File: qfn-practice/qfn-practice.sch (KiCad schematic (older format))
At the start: 5 parts, among them IC1 CY8C4245LQI-483, J1 Conn_01x10, J2 Conn_01x10, U1 ATtiny85-20MU, U2 STM32F031G4Ux

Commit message: map attiny pins to stm32 footprint
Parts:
- removed IC1: CY8C4245LQI-483, SamacSys_Parts:QFN50P600X600X60-41N-D, symbol SamacSys_Parts:CY8C4245LQI-483
- removed U1: ATtiny85-20MU, Package_DFN_QFN:QFN-20-1EP_4x4mm_P0.5mm_EP2.6x2.6mm, symbol MCU_Microchip_ATtiny:ATtiny85-20MU
- removed U2: STM32F031G4Ux, Package_DFN_QFN:QFN-28_4x4mm_P0.5mm, symbol MCU_ST_STM32F0:STM32F031G4Ux
- added U2: STM32F031G4Ux-thermal-pad, SamacSys_Parts:QFN28-4x4mm-0_5mmP-thermalpad, symbol SamacSys_Parts:STM32F031G4Ux-thermal-pad
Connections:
- net labels added: AT_GND_ST_PA5, AT_PB0_ST_GND, AT_PB1_ST_VDD, AT_PB2_ST_PA9, AT_PB3_ST_PF1, AT_PB4_ST_PA0, AT_PB5_ST_PF0, AT_VCC_ST_PA10
- wire segments 24 -> 33
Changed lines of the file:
@@
 $EndDescr
-$Comp
-L MCU_Microchip_ATtiny:ATtiny85-20MU U1
-U 1 1 60477C1D
-P 3050 1950
-F 0 "U1" H 2507 1996 50  0000 R CNN
-F 1 "ATtiny85-20MU" H 2507 1905 50  0000 R CNN
-F 2 "Package_DFN_QFN:QFN-20-1EP_4x4mm_P0.5mm_EP2.6x2.6mm" H 3050 1950 50  0001 C CIN
-F 3 "http://ww1.microchip.com/downloads/en/DeviceDoc/atmel-2586-avr-8-bit-microcontroller-attiny25-attiny45-attiny85_datasheet.pdf" H 3050 1950 50  0001 C CNN
-	1    3050 1950
-	1    0    0    -1
-$EndComp
-$Comp
-L MCU_ST_STM32F0:STM32F031G4Ux U2
-U 1 1 60479D04
-P 7150 3050
-F 0 "U2" H 7350 2100 50  0000 C CNN
-F 1 "STM32F031G4Ux" H 7600 2000 50  0000 C CNN
-F 2 "Package_DFN_QFN:QFN-28_4x4mm_P0.5mm" H 6750 2250 50  0001 R CNN
-F 3 "http://www.st.com/st-web-ui/static/active/en/resource/technical/document/datasheet/DM00104043.pdf" H 7150 3050 50  0001 C CNN
-	1    7150 3050
-	1    0    0    -1
-$EndComp
-$Comp
-L SamacSys_Parts:CY8C4245LQI-483 IC1
-U 1 1 6047907D
-P 2750 4900
-F 0 "IC1" H 4794 4496 50  0000 L CNN
-F 1 "CY8C4245LQI-483" H 4794 4405 50  0000 L CNN
-F 2 "SamacSys_Parts:QFN50P600X600X60-41N-D" H 4600 5700 50  0001 L CNN
-F 3 "http://www.cypress.com/file/138656/download.pdf" H 4600 5600 50  0001 L CNN
-F 4 "ARM Microcontrollers - MCU 32KB Flash 4KB SRAM PSoC 4" H 4600 5500 50  0001 L CNN "Description"
-F 5 "0.6" H 4600 5400 50  0001 L CNN "Height"
-F 6 "727-CY8C4245LQI-483" H 4600 5300 50  0001 L CNN "Mouser Part Number"
-F 7 "https://www.mouser.co.uk/ProductDetail/Cypress-Semiconductor/CY8C4245LQI-483?qs=LqwxS8kK3AsOWZFbGGtkOg%3D%3D" H 4600 5200 50  0001 L CNN "Mouser Price/Stock"
-F 8 "Cypress Semiconductor" H 4600 5100 50  0001 L CNN "Manufacturer_Name"
-F 9 "CY8C4245LQI-483" H 4600 5000 50  0001 L CNN "Manufacturer_Part_Number"
-	1    2750 4900
-	1    0    0    -1
-$EndComp
-$Comp
-L power:+3.3V #PWR0101
-U 1 1 6047A94E
-P 3050 1350
-F 0 "#PWR0101" H 3050 1200 50  0001 C CNN
-F 1 "+3.3V" H 3065 1523 50  0000 C CNN
-F 2 "" H 3050 1350 50  0001 C CNN
-F 3 "" H 3050 1350 50  0001 C CNN
-	1    3050 1350
-	1    0    0    -1
-$EndComp
 $Comp
 L power:+3.3V #PWR0102
 U 1 1 6047C05D
-P 7150 2250
-F 0 "#PWR0102" H 7150 2100 50  0001 C CNN
-F 1 "+3.3V" H 7165 2423 50  0000 C CNN
-F 2 "" H 7150 2250 50  0001 C CNN
-F 3 "" H 7150 2250 50  0001 C CNN
-	1    7150 2250
-	1    0    0    -1
-$EndComp
-$Comp
-L power:GND #PWR0103
-U 1 1 6047F4EF
-P 3050 2550
-F 0 "#PWR0103" H 3050 2300 50  0001 C CNN
-F 1 "GND" H 3055 2377 50  0000 C CNN
-F 2 "" H 3050 2550 50  0001 C CNN
-F 3 "" H 3050 2550 50  0001 C CNN
-	1    3050 2550
+P 7150 1800
+F 0 "#PWR0102" H 7150 1650 50  0001 C CNN
+F 1 "+3.3V" H 7165 1973 50  0000 C CNN
+F 2 "" H 7150 1800 50  0001 C CNN
+F 3 "" H 7150 1800 50  0001 C CNN
+	1    7150 1800
 	1    0    0    -1
 $EndComp
@@
 L power:GND #PWR0104
 U 1 1 60480964
-P 7150 3950
-F 0 "#PWR0104" H 7150 3700 50  0001 C CNN
-F 1 "GND" H 7155 3777 50  0000 C CNN
-F 2 "" H 7150 3950 50  0001 C CNN
-F 3 "" H 7150 3950 50  0001 C CNN
-	1    7150 3950
+P 7050 4100
+F 0 "#PWR0104" H 7050 3850 50  0001 C CNN
+F 1 "GND" H 7055 3927 50  0000 C CNN
+F 2 "" H 7050 4100 50  0001 C CNN
+F 3 "" H 7050 4100 50  0001 C CNN
+	1    7050 4100
 	1    0    0    -1
 $EndComp
-$Comp
-L power:GND #PWR0105
-U 1 1 604812EB
-P 2600 5900
-F 0 "#PWR0105" H 2600 5650 50  0001 C CNN
-F 1 "GND" H 2605 5727 50  0000 C CNN
-F 2 "" H 2600 5900 50  0001 C CNN
-F 3 "" H 2600 5900 50  0001 C CNN
-	1    2600 5900
-	1    0    0    -1
-$EndComp
-Wire Wire Line
-	2600 5900 2600 5700
-Wire Wire Line
-	2600 5700 2750 5700
 $Comp
 L Connector_Generic:Conn_01x10 J1
@@
 Text Label 7600 4850 0    50   ~ 0
 P19
+$Comp
+L SamacSys_Parts:STM32F031G4Ux-thermal-pad U2
+U 1 1 60570B22
+P 7150 3100
+F 0 "U2" H 6800 3900 50  0000 C CNN
+F 1 "STM32F031G4Ux-thermal-pad" H 7850 3900 50  0000 C CNN
+F 2 "SamacSys_Parts:QFN28-4x4mm-0_5mmP-thermalpad" H 7150 4450 50  0001 C CNN
+F 3 "" H 7150 4450 50  0001 C CNN
+	1    7150 3100
+	1    0    0    -1
+$EndComp
+Wire Wire Line
+	7650 3450 7850 3450
+Text Label 7850 3450 0    50   ~ 0
+AT_VCC_ST_PA10
+Wire Wire Line
+	7650 3350 7850 3350
+Text Label 7850 3350 0    50   ~ 0
+AT_PB2_ST_PA9
+Wire Wire Line
+	7650 2950 7850 2950
+Text Label 7850 2950 0    50   ~ 0
+AT_GND_ST_PA5
+Wire Wire Line
+	6650 2850 6450 2850
+Wire Wire Line
+	6450 2950 6650 2950
+Wire Wire Line
+	7650 2450 7850 2450
+Text Label 6450 2850 2    50   ~ 0
+AT_PB5_ST_PF0
+Text Label 6450 2950 2    50   ~ 0
+AT_PB3_ST_PF1
+Text Label 7850 2450 0    50   ~ 0
+AT_PB4_ST_PA0
+Wire Wire Line
+	7150 2250 7150 2100
+Wire Wire Line
+	7150 2100 7000 2100
+Text Label 7000 2100 2    50   ~ 0
+AT_PB1_ST_VDD
+Text Label 7300 4100 0    50   ~ 0
+AT_PB0_ST_GND
+Wire Wire Line
+	7150 4100 7150 3950
+Wire Wire Line
+	7150 4100 7300 4100
+Wire Wire Line
+	7050 3950 7050 4100
 $EndSCHEMATC

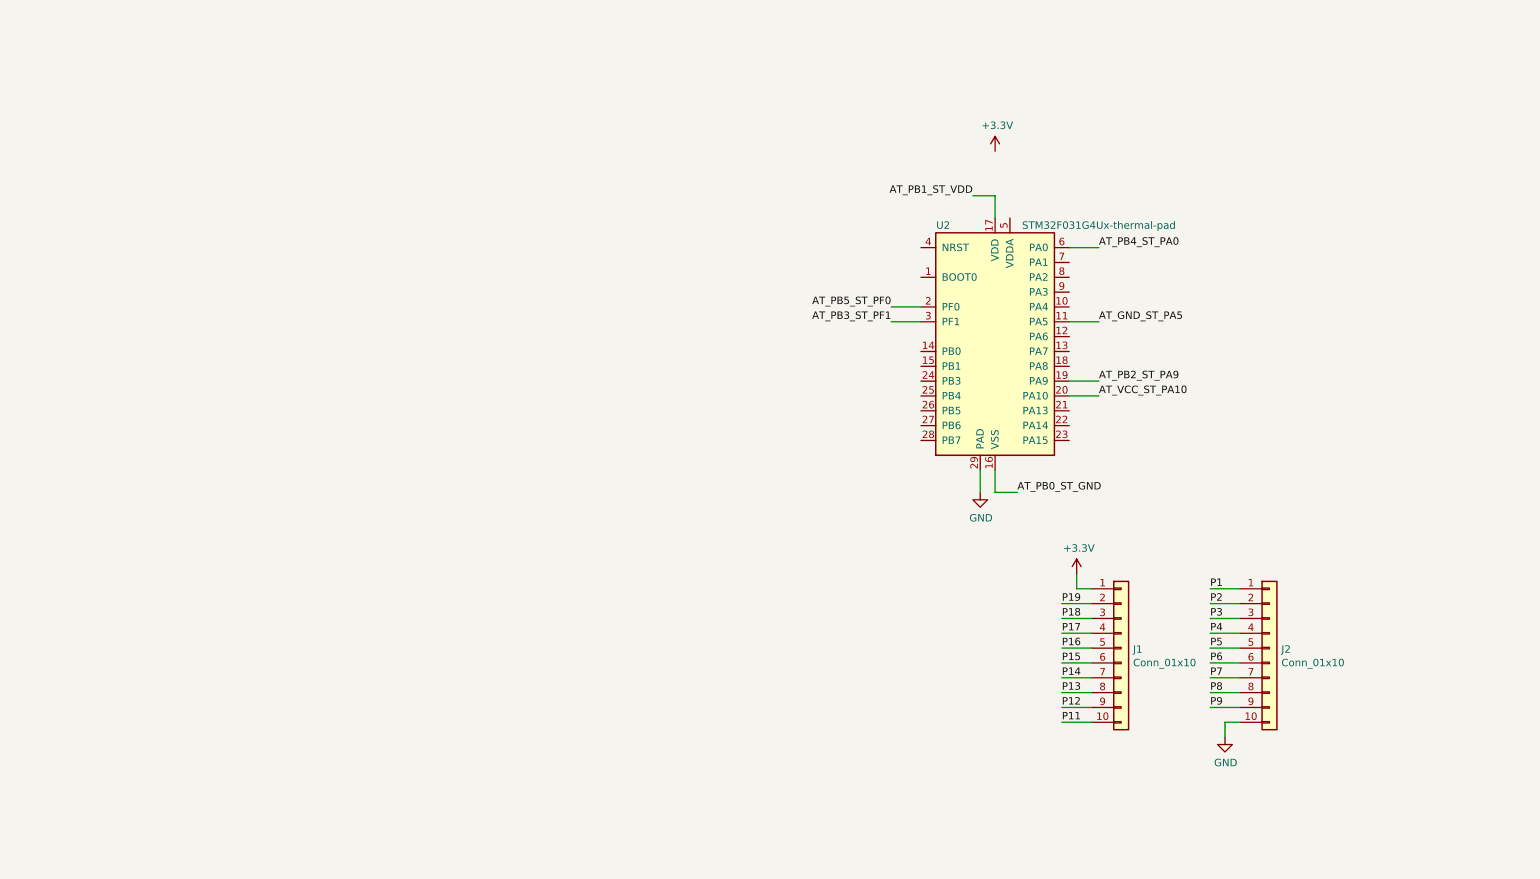
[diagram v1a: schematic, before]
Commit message: route to all side pins
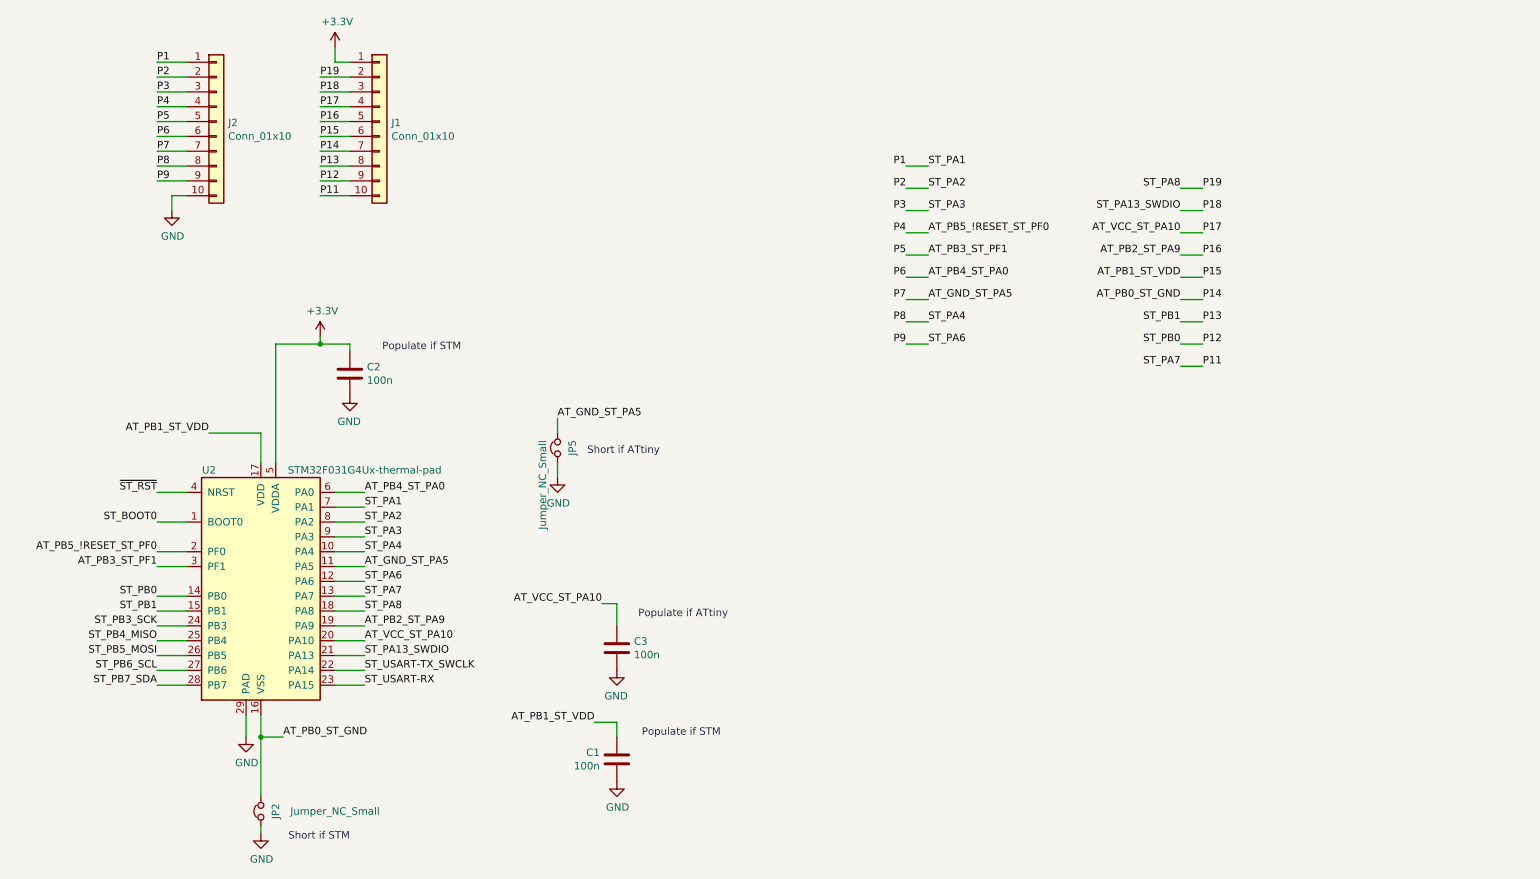
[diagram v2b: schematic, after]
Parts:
- added C1, C2, C3: 100n, SamacSys_Parts:RC-1206-0805-hybrid, symbol Device:C
- added JP2, JP5: Jumper_NC_Small, SamacSys_Parts:0202-solder-jumper, symbol Device:Jumper_NC_Small
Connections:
- net P14 is gone; now on net AT_PB0_ST_GND: J1.7 (Pin_7)
- net P15 is gone; now on net AT_PB1_ST_VDD: J1.6 (Pin_6)
- net P16 is gone; now on net AT_PB2_ST_PA9: J1.5 (Pin_5)
- net P17 is gone; now on net AT_VCC_ST_PA10: J1.4 (Pin_4)
- net P4 is gone; now on net AT_PB5_!RESET_ST_PF0: J2.4 (Pin_4)
- net P5 is gone; now on net AT_PB3_ST_PF1: J2.5 (Pin_5)
- net P6 is gone; now on net AT_PB4_ST_PA0: J2.6 (Pin_6)
- net P7 is gone; now on net AT_GND_ST_PA5: J2.7 (Pin_7)
- net +3V3: now also U2.5 (VDDA), C2.2
- net AT_GND_ST_PA5: now also JP5.2
- net AT_PB0_ST_GND: now also JP2.2
- net AT_PB1_ST_VDD: now also C1.2
- net AT_VCC_ST_PA10: now also C3.2
- net GND: now also C1.1, C2.1, C3.1, JP2.1, JP5.1
- net P1: now also U2.7 (PA1)
- net P11: now also U2.13 (PA7)
- net P12: now also U2.14 (PB0)
- net P13: now also U2.15 (PB1)
- net P18: now also U2.21 (PA13)
- net P19: now also U2.18 (PA8)
- net P2: now also U2.8 (PA2)
- net P3: now also U2.9 (PA3)
- net P8: now also U2.10 (PA4)
- net P9: now also U2.12 (PA6)
- net ST_BOOT0: now reaches U2.1 (BOOT0)
- net ST_USART-TX_SWCLK: now reaches U2.22 (PA14)
- net ST_USART-RX: now reaches U2.23 (PA15)
- net ST_PB3_SCK: now reaches U2.24 (PB3)
- net ST_PB4_MISO: now reaches U2.25 (PB4)
- net ST_PB5_MOSI: now reaches U2.26 (PB5)
- net ST_PB6_SCL: now reaches U2.27 (PB6)
- net ST_PB7_SDA: now reaches U2.28 (PB7)
- net ~ST_RST: now reaches U2.4 (NRST)
- net AT_PB5_ST_PF0 renamed AT_PB5_!RESET_ST_PF0
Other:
- note added: "Populate if ATtiny\n"
- note added: "Populate if STM"
- note added: "Populate if STM\n"
- note added: "Short if ATtiny"
- note added: "Short if STM\n"
- moved on the sheet: J1, J2, U2

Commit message: add headers for programming etc
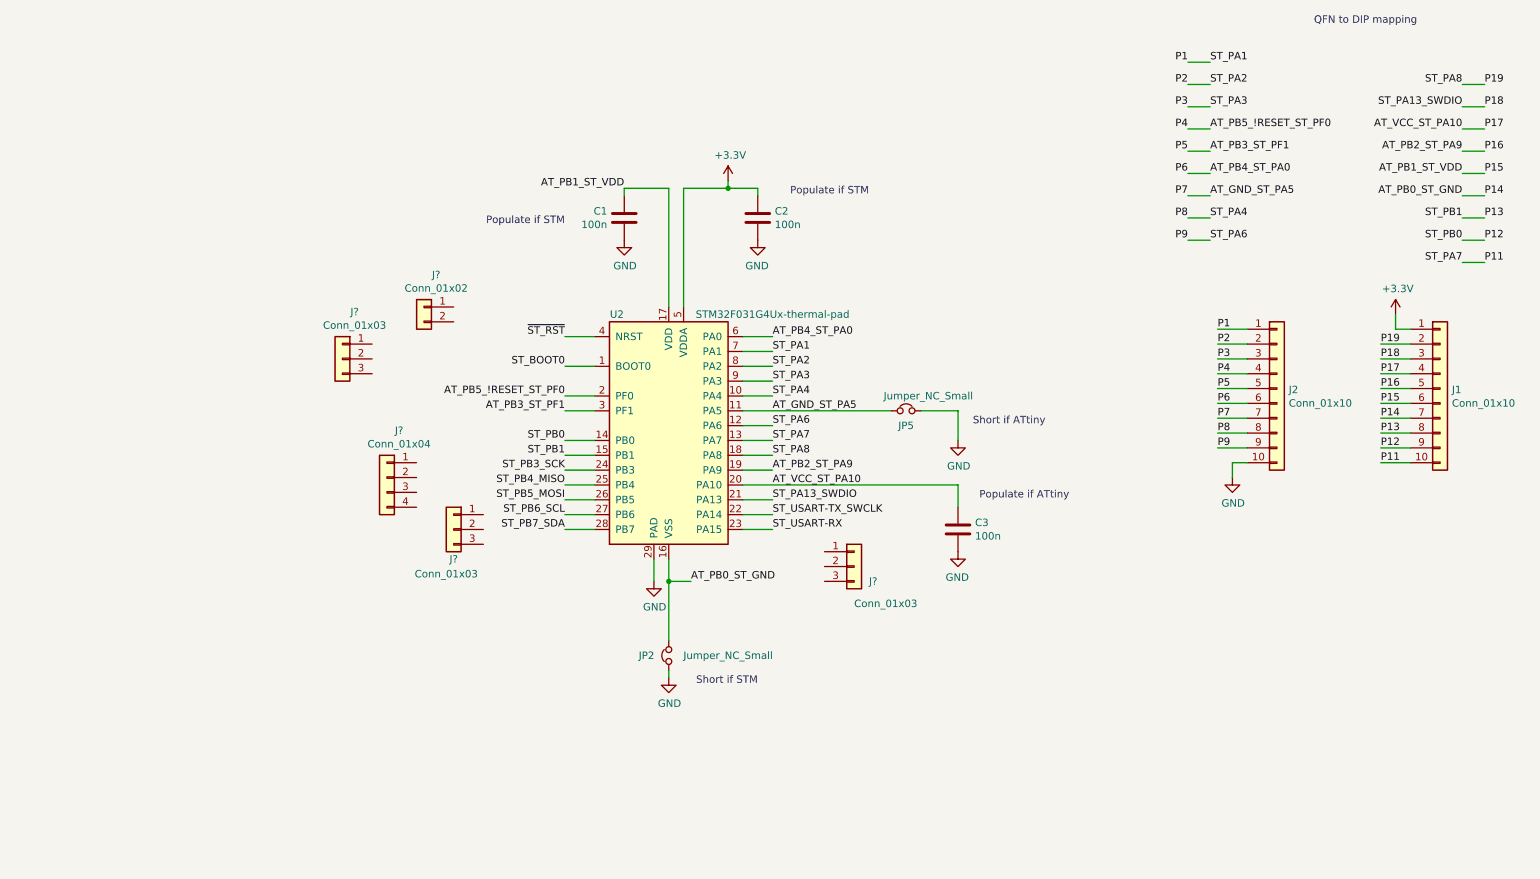
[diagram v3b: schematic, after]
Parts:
- added J?: Conn_01x02, symbol Connector_Generic:Conn_01x02
- added J? (x3): Conn_01x03, symbol Connector_Generic:Conn_01x03
- added J?: Conn_01x04, symbol Connector_Generic:Conn_01x04
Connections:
- net AT_GND_ST_PA5: now also JP5.1; no longer JP5.2
- net GND: now also JP5.2; no longer JP5.1
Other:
- note added: "QFN to DIP mapping\n"
- moved on the sheet: C1, C2, C3, J1, J2, JP2, JP5, U2
